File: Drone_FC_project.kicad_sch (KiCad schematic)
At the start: 1 part

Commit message: resistor
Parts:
- added R1: R, symbol Device:R
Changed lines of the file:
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@@
 	(paper "A4")
+	(symbol
+		(lib_id "Device:R")
+		(at 173.99 99.06 0)
+		(unit 1)
+		(body_style 1)
+		(exclude_from_sim no)
+		(in_bom yes)
+		(on_board yes)
+		(in_pos_files yes)
+		(dnp no)
+		(fields_autoplaced yes)
+		(property "Reference" "R1"
+			(at 176.53 97.7899 0)
+			(show_name no)
+			(do_not_autoplace no)
+			(effects
+				(font
+					(size 1.27 1.27)
+				)
+				(justify left)
+			)
+		)
+		(property "Value" "R"
+			(at 176.53 100.3299 0)
+			(show_name no)
+			(do_not_autoplace no)
+			(effects
+				(font
+					(size 1.27 1.27)
+				)
+				(justify left)
+			)
+		)
+		(property "Footprint" ""
+			(at 172.212 99.06 90)
+			(hide yes)
+			(show_name no)
+			(do_not_autoplace no)
+			(effects
+				(font
+					(size 1.27 1.27)
+				)
+			)
+		)
+		(property "Datasheet" ""
+			(at 173.99 99.06 0)
+			(hide yes)
+			(show_name no)
+			(do_not_autoplace no)
+			(effects
+				(font
+					(size 1.27 1.27)
+				)
+			)
+		)
+		(property "Description" "Resistor"
+			(at 173.99 99.06 0)
+			(hide yes)
+			(show_name no)
+			(do_not_autoplace no)
+			(effects
+				(font
+					(size 1.27 1.27)
+				)
+			)
+		)
+		(pin "1"
+		)
+		(pin "2"
+		)
+		(instances
+			(project "Drone_FC_project"
+				(path "/3077c137-9a1a-496f-be15-3587b3336d21"
+					(reference "R1")
+					(unit 1)
+				)
+			)
+		)
+	)
 	(symbol
 		(lib_id "power:GND")

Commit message: m hole
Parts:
- added H2: MountingHole, symbol Mechanical:MountingHole
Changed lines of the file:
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@@
+	)
+	(symbol
+		(lib_id "Mechanical:MountingHole")
+		(at 114.2999 127.3769 0)
+		(unit 1)
+		(body_style 1)
+		(exclude_from_sim no)
+		(in_bom no)
+		(on_board yes)
+		(in_pos_files yes)
+		(dnp no)
+		(fields_autoplaced yes)
+		(property "Reference" "H2"
+			(at 116.8399 126.1068 0)
+			(show_name no)
+			(do_not_autoplace no)
+			(effects
+				(font
+					(size 1.27 1.27)
+				)
+				(justify left)
+			)
+		)
+		(property "Value" "MountingHole"
+			(at 116.8399 128.6468 0)
+			(show_name no)
+			(do_not_autoplace no)
+			(effects
+				(font
+					(size 1.27 1.27)
+				)
+				(justify left)
+			)
+		)
+		(property "Footprint" ""
+			(at 114.2999 127.3769 0)
+			(hide yes)
+			(show_name no)
+			(do_not_autoplace no)
+			(effects
+				(font
+					(size 1.27 1.27)
+				)
+			)
+		)
+		(property "Datasheet" ""
+			(at 114.2999 127.3769 0)
+			(hide yes)
+			(show_name no)
+			(do_not_autoplace no)
+			(effects
+				(font
+					(size 1.27 1.27)
+				)
+			)
+		)
+		(property "Description" "Mounting Hole without connection"
+			(at 114.2999 127.3769 0)
+			(hide yes)
+			(show_name no)
+			(do_not_autoplace no)
+			(effects
+				(font
+					(size 1.27 1.27)
+				)
+			)
+		)
+		(instances
+			(project "Drone_FC_project"
+				(path "/3077c137-9a1a-496f-be15-3587b3336d21"
+					(reference "H2")
+					(unit 1)
+				)
+			)
+		)
 	)
 	(symbol

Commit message: imu
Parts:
- removed H2: MountingHole, symbol Mechanical:MountingHole
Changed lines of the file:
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@@
-	)
-	(symbol
-		(lib_id "Mechanical:MountingHole")
-		(at 114.2999 127.3769 0)
-		(unit 1)
-		(body_style 1)
-		(exclude_from_sim no)
-		(in_bom no)
-		(on_board yes)
-		(in_pos_files yes)
-		(dnp no)
-		(fields_autoplaced yes)
-		(property "Reference" "H2"
-			(at 116.8399 126.1068 0)
-			(show_name no)
-			(do_not_autoplace no)
-			(effects
-				(font
-					(size 1.27 1.27)
-				)
-				(justify left)
-			)
-		)
-		(property "Value" "MountingHole"
-			(at 116.8399 128.6468 0)
-			(show_name no)
-			(do_not_autoplace no)
-			(effects
-				(font
-					(size 1.27 1.27)
-				)
-				(justify left)
-			)
-		)
-		(property "Footprint" ""
-			(at 114.2999 127.3769 0)
-			(hide yes)
-			(show_name no)
-			(do_not_autoplace no)
-			(effects
-				(font
-					(size 1.27 1.27)
-				)
-			)
-		)
-		(property "Datasheet" ""
-			(at 114.2999 127.3769 0)
-			(hide yes)
-			(show_name no)
-			(do_not_autoplace no)
-			(effects
-				(font
-					(size 1.27 1.27)
-				)
-			)
-		)
-		(property "Description" "Mounting Hole without connection"
-			(at 114.2999 127.3769 0)
-			(hide yes)
-			(show_name no)
-			(do_not_autoplace no)
-			(effects
-				(font
-					(size 1.27 1.27)
-				)
-			)
-		)
-		(instances
-			(project "Drone_FC_project"
-				(path "/3077c137-9a1a-496f-be15-3587b3336d21"
-					(reference "H2")
-					(unit 1)
-				)
-			)
-		)
 	)
 	(symbol

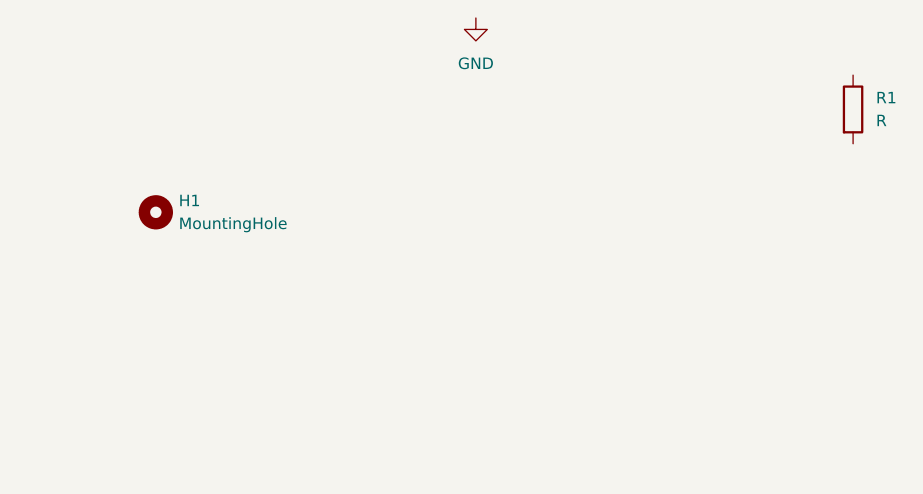
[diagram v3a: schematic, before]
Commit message: created four sublevel schematics (battery, motors, IMU, radio)
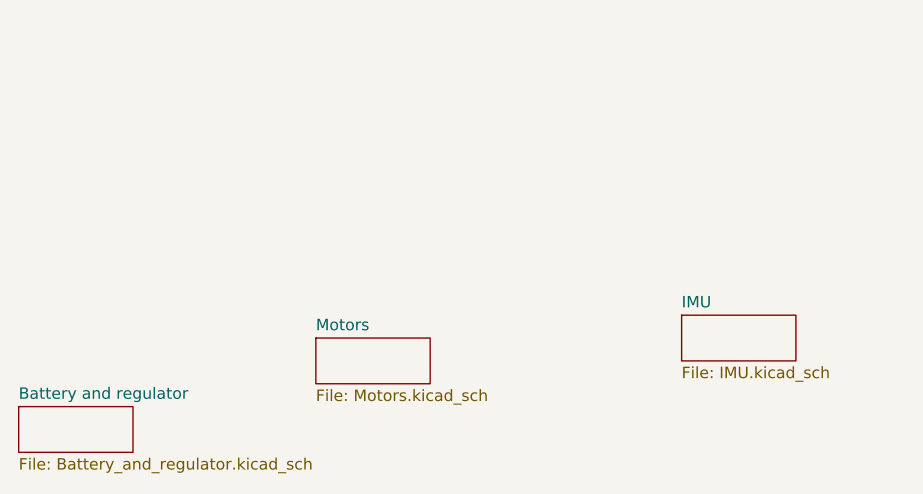
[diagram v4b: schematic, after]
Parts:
- removed H1: MountingHole, symbol Mechanical:MountingHole
- removed R1: R, symbol Device:R
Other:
- added sheet Battery and regulator (Battery_and_regulator.kicad_sch)
- added sheet IMU (IMU.kicad_sch)
- added sheet Motors (Motors.kicad_sch)
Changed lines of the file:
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@@
 	(generator_version "10.0")
 	(paper "A4")
-	(symbol
-		(lib_id "Device:R")
-		(at 173.99 99.06 0)
-		(unit 1)
-		(body_style 1)
+	(sheet
+		(at 114.3 124.46)
+		(size 12.7 5.08)
 		(exclude_from_sim no)
 		(in_bom yes)
 		(on_board yes)
-		(in_pos_files yes)
 		(dnp no)
 		(fields_autoplaced yes)
-		(property "Reference" "R1"
-			(at 176.53 97.7899 0)
+		(stroke
+			(width 0.1524)
+			(type solid)
+		)
+		(fill
+			(color 0 0 0 0)
+		)
+		(property "Sheetname" "Motors"
+			(at 114.3 123.7484 0)
 			(show_name no)
 			(do_not_autoplace no)
@@
 					(size 1.27 1.27)
 				)
-				(justify left)
+				(justify left bottom)
 			)
 		)
-		(property "Value" "R"
-			(at 176.53 100.3299 0)
+		(property "Sheetfile" "Motors.kicad_sch"
+			(at 114.3 130.1246 0)
 			(show_name no)
 			(do_not_autoplace no)
@@
 					(size 1.27 1.27)
 				)
-				(justify left)
+				(justify left top)
 			)
 		)
-		(property "Footprint" ""
-			(at 172.212 99.06 90)
-			(hide yes)
+		(instances
+			(project "Drone_FC_project"
+				(path "/3077c137-9a1a-496f-be15-3587b3336d21"
+					(page "3")
+				)
+			)
+		)
+	)
+	(sheet
+		(at 81.28 132.08)
+		(size 12.7 5.08)
+		(exclude_from_sim no)
+		(in_bom yes)
+		(on_board yes)
+		(dnp no)
+		(fields_autoplaced yes)
+		(stroke
+			(width 0.1524)
+			(type solid)
+		)
+		(fill
+			(color 0 0 0 0)
+		)
+		(property "Sheetname" "Battery and regulator"
+			(at 81.28 131.3684 0)
 			(show_name no)
 			(do_not_autoplace no)
@@
 					(size 1.27 1.27)
 				)
+				(justify left bottom)
 			)
 		)
-		(property "Datasheet" ""
-			(at 173.99 99.06 0)
-			(hide yes)
+		(property "Sheetfile" "Battery_and_regulator.kicad_sch"
+			(at 81.28 137.7446 0)
 			(show_name no)
 			(do_not_autoplace no)
@@
 					(size 1.27 1.27)
 				)
+				(justify left top)
 			)
 		)
-		(property "Description" "Resistor"
-			(at 173.99 99.06 0)
-			(hide yes)
+		(instances
+			(project "Drone_FC_project"
+				(path "/3077c137-9a1a-496f-be15-3587b3336d21"
+					(page "4")
+				)
+			)
+		)
+	)
+	(sheet
+		(at 154.94 121.92)
+		(size 12.7 5.08)
+		(exclude_from_sim no)
+		(in_bom yes)
+		(on_board yes)
+		(dnp no)
+		(fields_autoplaced yes)
+		(stroke
+			(width 0.1524)
+			(type solid)
+		)
+		(fill
+			(color 0 0 0 0)
+		)
+		(property "Sheetname" "IMU"
+			(at 154.94 121.2084 0)
 			(show_name no)
 			(do_not_autoplace no)
@@
 					(size 1.27 1.27)
 				)
+				(justify left bottom)
 			)
 		)
-		(pin "1"
-		)
-		(pin "2"
-		)
-		(instances
-			(project "Drone_FC_project"
-				(path "/3077c137-9a1a-496f-be15-3587b3336d21"
-					(reference "R1")
-					(unit 1)
-				)
-			)
-		)
-	)
-	(symbol
-		(lib_id "power:GND")
-		(at 132.08 88.9 0)
-		(unit 1)
-		(body_style 1)
-		(exclude_from_sim no)
-		(in_bom yes)
-		(on_board yes)
-		(in_pos_files yes)
-		(dnp no)
-		(fields_autoplaced yes)
-		(property "Reference" "#PWR01"
-			(at 132.08 95.25 0)
-			(hide yes)
+		(property "Sheetfile" "IMU.kicad_sch"
+			(at 154.94 127.5846 0)
 			(show_name no)
 			(do_not_autoplace no)
@@
 					(size 1.27 1.27)
 				)
-			)
-		)
-		(property "Value" "GND"
-			(at 132.08 93.98 0)
-			(show_name no)
-			(do_not_autoplace no)
-			(effects
-				(font
-					(size 1.27 1.27)
-				)
-			)
-		)
-		(property "Footprint" ""
-			(at 132.08 88.9 0)
-			(hide yes)
-			(show_name no)
-			(do_not_autoplace no)
-			(effects
-				(font
-					(size 1.27 1.27)
-				)
-			)
-		)
-		(property "Datasheet" ""
-			(at 132.08 88.9 0)
-			(hide yes)
-			(show_name no)
-			(do_not_autoplace no)
-			(effects
-				(font
-					(size 1.27 1.27)
-				)
-			)
-		)
-		(property "Description" "Power symbol creates a global label with name \"GND\" , ground"
-			(at 132.08 88.9 0)
-			(hide yes)
-			(show_name no)
-			(do_not_autoplace no)
-			(effects
-				(font
-					(size 1.27 1.27)
-				)
-			)
-		)
-		(pin "1"
-		)
-		(instances
-			(project "Drone_FC_project"
-				(path "/3077c137-9a1a-496f-be15-3587b3336d21"
-					(reference "#PWR01")
-					(unit 1)
-				)
-			)
-		)
-	)
-	(symbol
-		(lib_id "Mechanical:MountingHole")
-		(at 96.52 110.49 0)
-		(unit 1)
-		(body_style 1)
-		(exclude_from_sim no)
-		(in_bom no)
-		(on_board yes)
-		(in_pos_files yes)
-		(dnp no)
-		(fields_autoplaced yes)
-		(property "Reference" "H1"
-			(at 99.06 109.2199 0)
-			(show_name no)
-			(do_not_autoplace no)
-			(effects
-				(font
-					(size 1.27 1.27)
-				)
-				(justify left)
-			)
-		)
-		(property "Value" "MountingHole"
-			(at 99.06 111.7599 0)
-			(show_name no)
-			(do_not_autoplace no)
-			(effects
-				(font
-					(size 1.27 1.27)
-				)
-				(justify left)
-			)
-		)
-		(property "Footprint" ""
-			(at 96.52 110.49 0)
-			(hide yes)
-			(show_name no)
-			(do_not_autoplace no)
-			(effects
-				(font
-					(size 1.27 1.27)
-				)
-			)
-		)
-		(property "Datasheet" ""
-			(at 96.52 110.49 0)
-			(hide yes)
-			(show_name no)
-			(do_not_autoplace no)
-			(effects
-				(font
-					(size 1.27 1.27)
-				)
-			)
-		)
-		(property "Description" "Mounting Hole without connection"
-			(at 96.52 110.49 0)
-			(hide yes)
-			(show_name no)
-			(do_not_autoplace no)
-			(effects
-				(font
-					(size 1.27 1.27)
-				)
+				(justify left top)
 			)
 		)
@@
 			(project "Drone_FC_project"
 				(path "/3077c137-9a1a-496f-be15-3587b3336d21"
-					(reference "H1")
-					(unit 1)
+					(page "2")
 				)
 			)

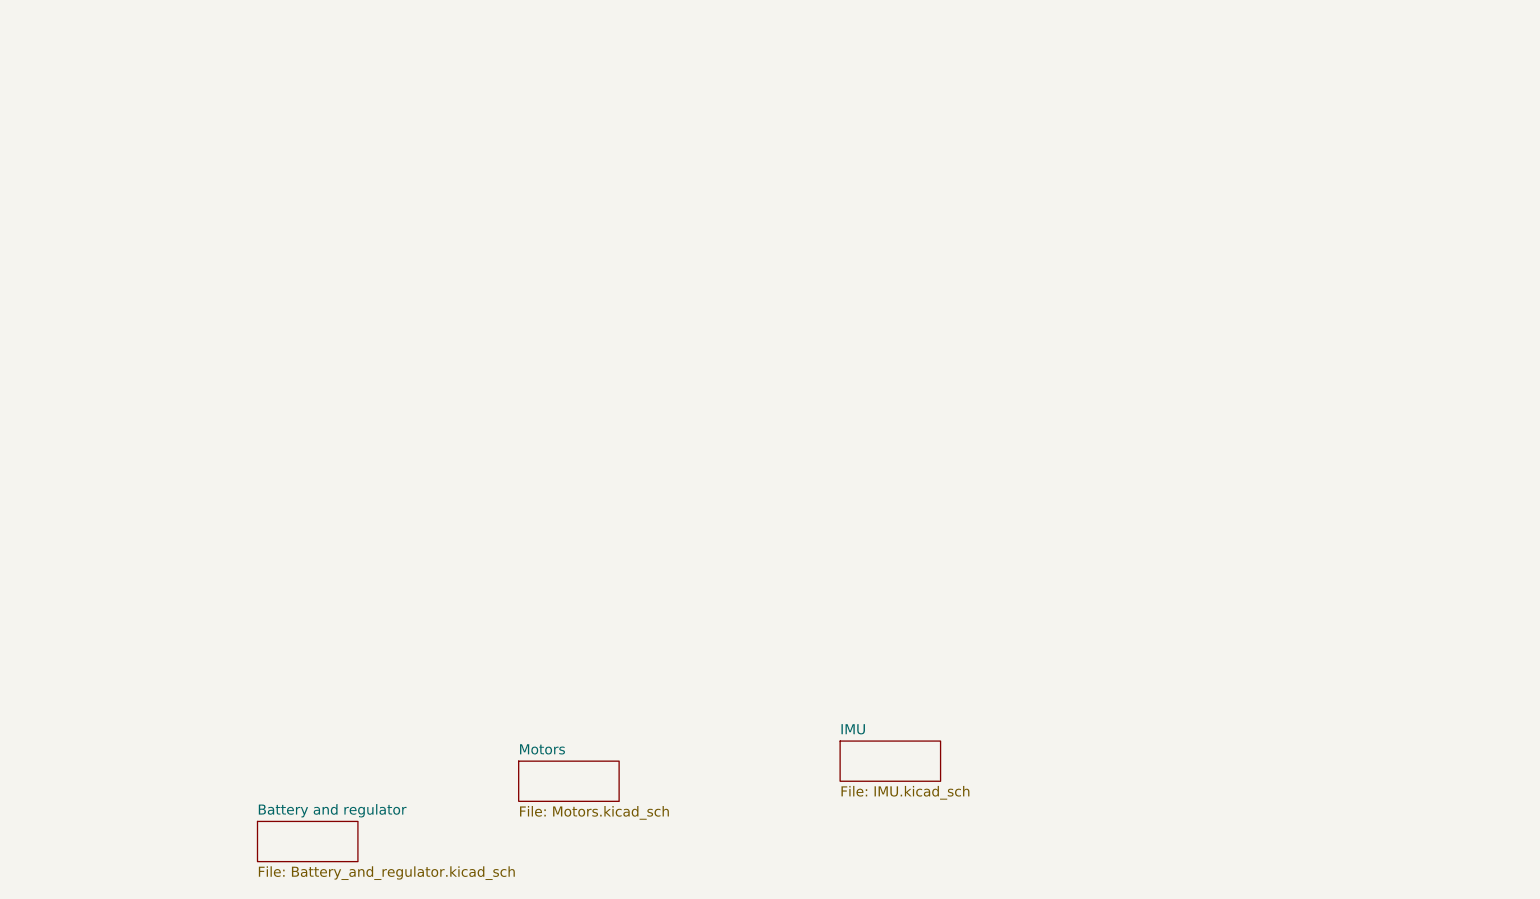
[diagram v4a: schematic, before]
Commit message: filled in the four MOSFETS for motor control
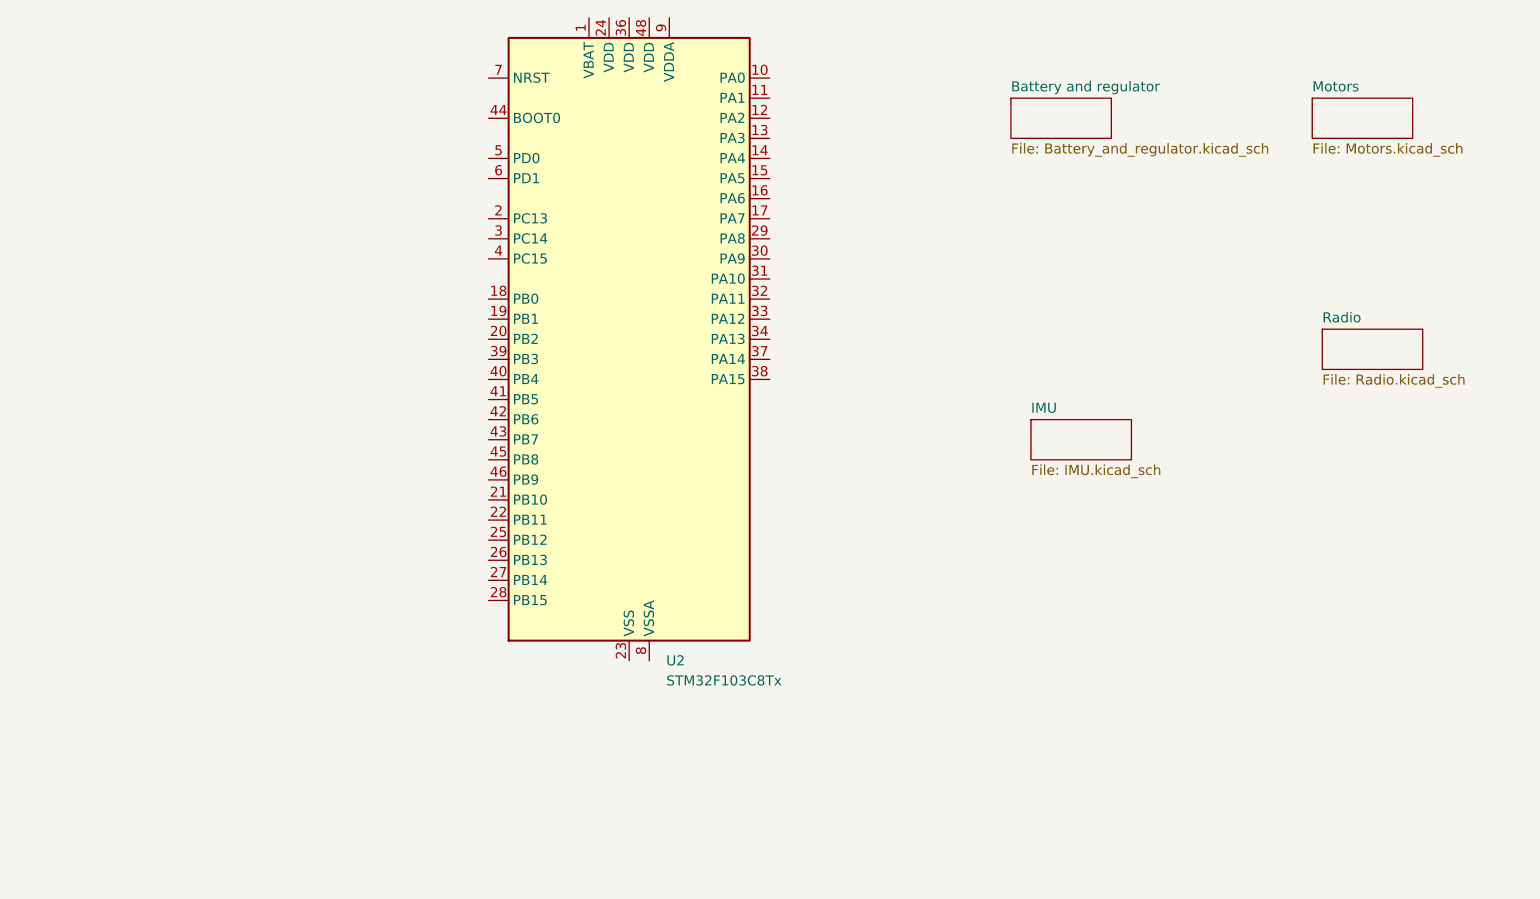
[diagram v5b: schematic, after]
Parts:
- added U2: STM32F103C8Tx, Package_QFP:LQFP-48_7x7mm_P0.5mm, symbol MCU_ST_STM32F1:STM32F103C8Tx
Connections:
- new net: U2.23 (VSS), U2.35 (VSS), U2.47 (VSS)
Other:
- added sheet Radio (Radio.kicad_sch)
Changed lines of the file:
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@@
 	(generator_version "10.0")
 	(paper "A4")
+	(symbol
+		(lib_id "MCU_ST_STM32F1:STM32F103C8Tx")
+		(at 128.27 71.12 0)
+		(unit 1)
+		(body_style 1)
+		(exclude_from_sim no)
+		(in_bom yes)
+		(on_board yes)
+		(in_pos_files yes)
+		(dnp no)
+		(fields_autoplaced yes)
+		(property "Reference" "U2"
+			(at 132.9533 111.76 0)
+			(show_name no)
+			(do_not_autoplace no)
+			(effects
+				(font
+					(size 1.27 1.27)
+				)
+				(justify left)
+			)
+		)
+		(property "Value" "STM32F103C8Tx"
+			(at 132.9533 114.3 0)
+			(show_name no)
+			(do_not_autoplace no)
+			(effects
+				(font
+					(size 1.27 1.27)
+				)
+				(justify left)
+			)
+		)
+		(property "Footprint" "Package_QFP:LQFP-48_7x7mm_P0.5mm"
+			(at 113.03 109.22 0)
+			(hide yes)
+			(show_name no)
+			(do_not_autoplace no)
+			(effects
+				(font
+					(size 1.27 1.27)
+				)
+				(justify right)
+			)
+		)
+		(property "Datasheet" "https://www.st.com/resource/en/datasheet/stm32f103c8.pdf"
+			(at 128.27 71.12 0)
+			(hide yes)
+			(show_name no)
+			(do_not_autoplace no)
+			(effects
+				(font
+					(size 1.27 1.27)
+				)
+			)
+		)
+		(property "Description" "STMicroelectronics Arm Cortex-M3 MCU, 64KB flash, 20KB RAM, 72 MHz, 2.0-3.6V, 37 GPIO, LQFP48"
+			(at 128.27 71.12 0)
+			(hide yes)
+			(show_name no)
+			(do_not_autoplace no)
+			(effects
+				(font
+					(size 1.27 1.27)
+				)
+			)
+		)
+		(pin "3"
+		)
+		(pin "8"
+		)
+		(pin "6"
+		)
+		(pin "5"
+		)
+		(pin "10"
+		)
+		(pin "4"
+		)
+		(pin "2"
+		)
+		(pin "12"
+		)
+		(pin "7"
+		)
+		(pin "11"
+		)
+		(pin "9"
+		)
+		(pin "1"
+		)
+		(pin "13"
+		)
+		(pin "15"
+		)
+		(pin "31"
+		)
+		(pin "23"
+		)
+		(pin "29"
+		)
+		(pin "16"
+		)
+		(pin "35"
+		)
+		(pin "37"
+		)
+		(pin "18"
+		)
+		(pin "27"
+		)
+		(pin "32"
+		)
+		(pin "19"
+		)
+		(pin "38"
+		)
+		(pin "28"
+		)
+		(pin "43"
+		)
+		(pin "36"
+		)
+		(pin "39"
+		)
+		(pin "42"
+		)
+		(pin "20"
+		)
+		(pin "21"
+		)
+		(pin "41"
+		)
+		(pin "24"
+		)
+		(pin "40"
+		)
+		(pin "33"
+		)
+		(pin "45"
+		)
+		(pin "14"
+		)
+		(pin "44"
+		)
+		(pin "30"
+		)
+		(pin "25"
+		)
+		(pin "22"
+		)
+		(pin "17"
+		)
+		(pin "26"
+		)
+		(pin "34"
+		)
+		(pin "47"
+		)
+		(pin "48"
+		)
+		(pin "46"
+		)
+		(instances
+			(project "Drone_FC_project"
+				(path "/3077c137-9a1a-496f-be15-3587b3336d21"
+					(reference "U2")
+					(unit 1)
+				)
+			)
+		)
+	)
 	(sheet
-		(at 114.3 124.46)
+		(at 214.63 40.64)
 		(size 12.7 5.08)
 		(exclude_from_sim no)
@@
 		)
 		(property "Sheetname" "Motors"
-			(at 114.3 123.7484 0)
+			(at 214.63 39.9284 0)
 			(show_name no)
 			(do_not_autoplace no)
@@
 		)
 		(property "Sheetfile" "Motors.kicad_sch"
-			(at 114.3 130.1246 0)
+			(at 214.63 46.3046 0)
 			(show_name no)
 			(do_not_autoplace no)
@@
 	)
 	(sheet
-		(at 81.28 132.08)
+		(at 176.53 40.64)
 		(size 12.7 5.08)
 		(exclude_from_sim no)
@@
 		)
 		(property "Sheetname" "Battery and regulator"
-			(at 81.28 131.3684 0)
+			(at 176.53 39.9284 0)
 			(show_name no)
 			(do_not_autoplace no)
@@
 		)
 		(property "Sheetfile" "Battery_and_regulator.kicad_sch"
-			(at 81.28 137.7446 0)
+			(at 176.53 46.3046 0)
 			(show_name no)
 			(do_not_autoplace no)
@@
 	)
 	(sheet
-		(at 154.94 121.92)
+		(at 215.9 69.85)
 		(size 12.7 5.08)
 		(exclude_from_sim no)
@@
 			(color 0 0 0 0)
 		)
+		(property "Sheetname" "Radio"
+			(at 215.9 69.1384 0)
+			(show_name no)
+			(do_not_autoplace no)
+			(effects
+				(font
+					(size 1.27 1.27)
+				)
+				(justify left bottom)
+			)
+		)
+		(property "Sheetfile" "Radio.kicad_sch"
+			(at 215.9 75.5146 0)
+			(show_name no)
+			(do_not_autoplace no)
+			(effects
+				(font
+					(size 1.27 1.27)
+				)
+				(justify left top)
+			)
+		)
+		(instances
+			(project "Drone_FC_project"
+				(path "/3077c137-9a1a-496f-be15-3587b3336d21"
+					(page "5")
+				)
+			)
+		)
+	)
+	(sheet
+		(at 179.07 81.28)
+		(size 12.7 5.08)
+		(exclude_from_sim no)
+		(in_bom yes)
+		(on_board yes)
+		(dnp no)
+		(fields_autoplaced yes)
+		(stroke
+			(width 0.1524)
+			(type solid)
+		)
+		(fill
+			(color 0 0 0 0)
+		)
 		(property "Sheetname" "IMU"
-			(at 154.94 121.2084 0)
+			(at 179.07 80.5684 0)
 			(show_name no)
 			(do_not_autoplace no)
@@
 		)
 		(property "Sheetfile" "IMU.kicad_sch"
-			(at 154.94 127.5846 0)
-			(show_name no)
-			(do_not_autoplace no)
+			(at 179.07 86.9446 0)
+			(show_name no)
+			(do_not_autoplace no)
